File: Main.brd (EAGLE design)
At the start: 100 x 80 mm, 27 parts, among them U1 L298, U2 LM 1084 IT5,0, U3 LM 1084 IT3,3, U4 L298, X1 Motors, X3 Battery

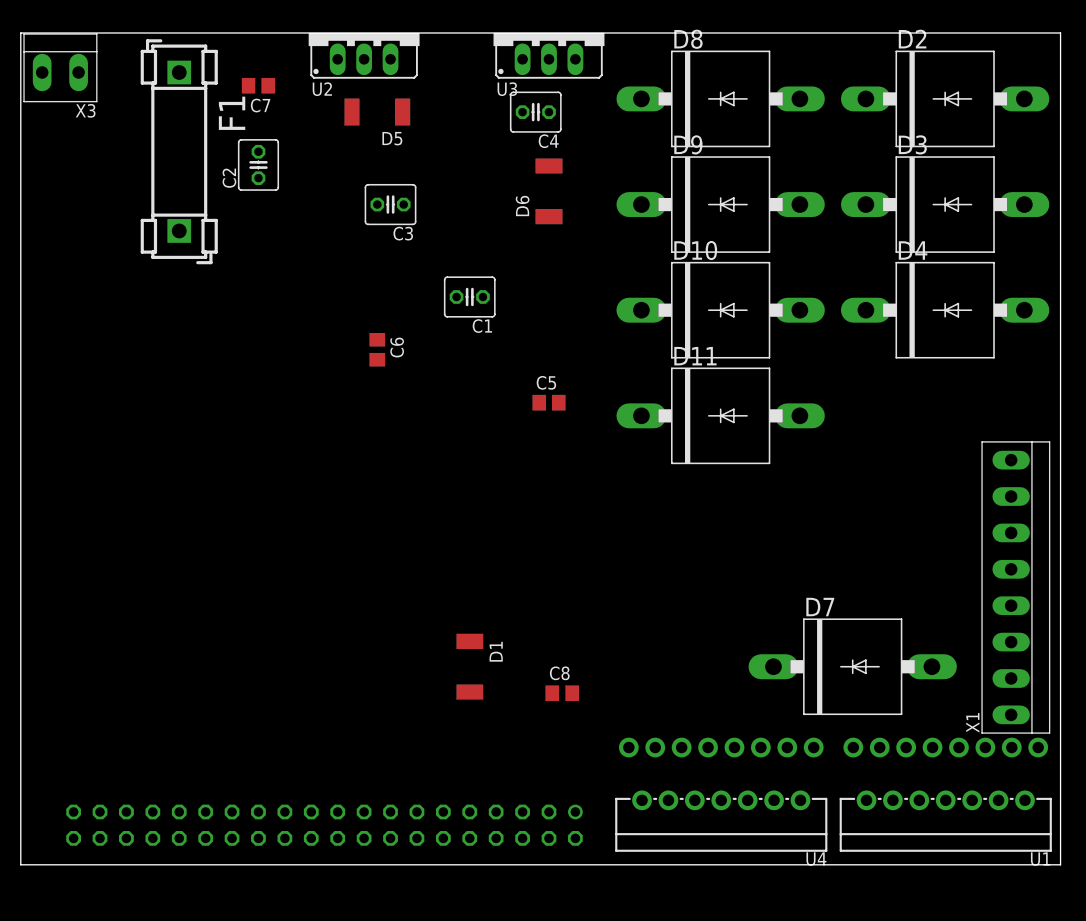
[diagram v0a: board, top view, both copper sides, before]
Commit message: got board working again
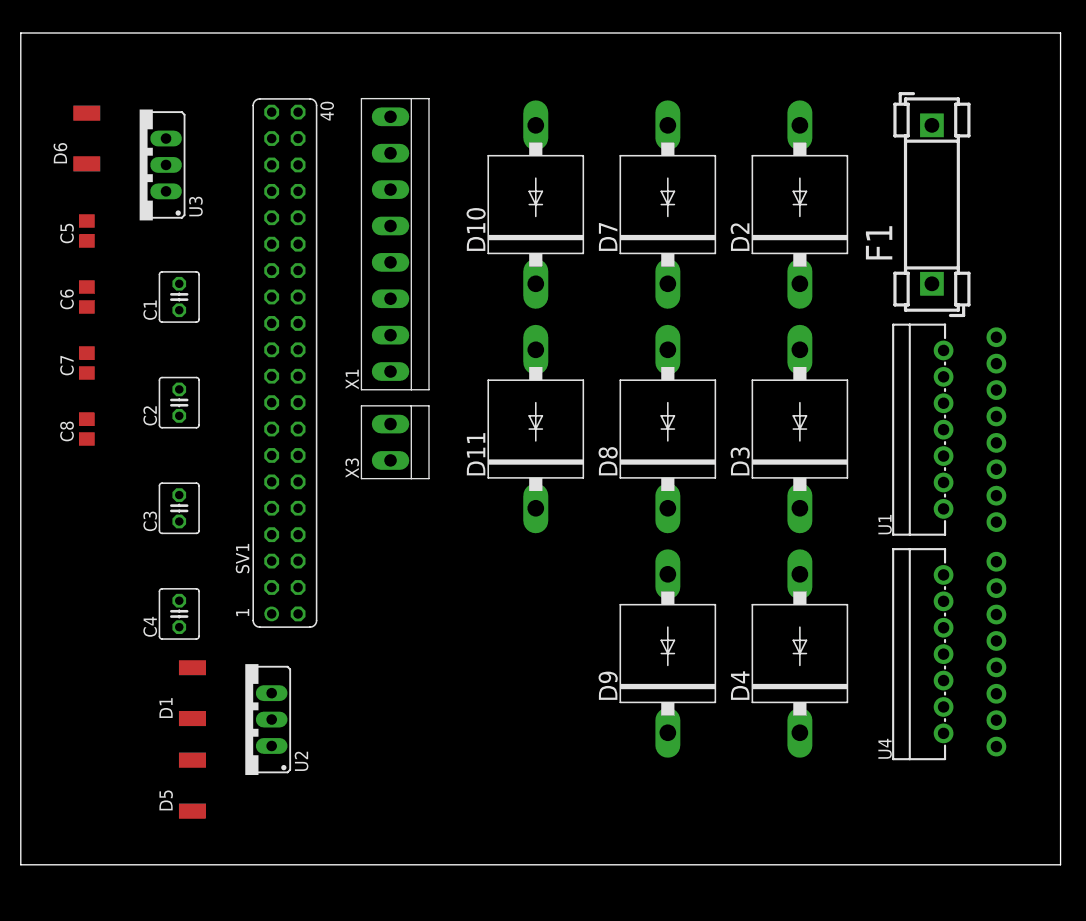
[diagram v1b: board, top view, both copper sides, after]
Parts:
- moved F1 75.2 mm to (87.6, 55.9), turned to 90 degrees
- moved X1 68.2 mm to (35.6, 59.7)
- moved D5 67.2 mm to (16.5, 7.62), turned to 90 degrees
- moved U2 67.0 mm to (21.6, 14.0), turned to 90 degrees
- moved C4 59.2 mm to (15.2, 24.1), turned to 90 degrees
- moved C8 52.3 mm to (6.35, 41.9), turned to 90 degrees
- moved D7 47.9 mm to (62.2, 63.5), turned to 90 degrees
- moved X3 47.7 mm to (35.6, 40.6), turned to 90 degrees
- moved C5 47.4 mm to (6.35, 61.0), turned to 90 degrees
- moved D6 44.7 mm to (6.35, 69.8)
- moved SV1 44.6 mm to (25.4, 48.3), flipped to the top, turned to 90 degrees
- moved D9 43.5 mm to (62.2, 20.3), turned to 90 degrees
- moved U3 41.4 mm to (11.4, 67.3), turned to 90 degrees
- moved D4 35.9 mm to (74.9, 20.3), turned to 90 degrees
- moved C3 35.6 mm to (15.2, 34.3), turned to 90 degrees
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
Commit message: better protection for reverse polarity
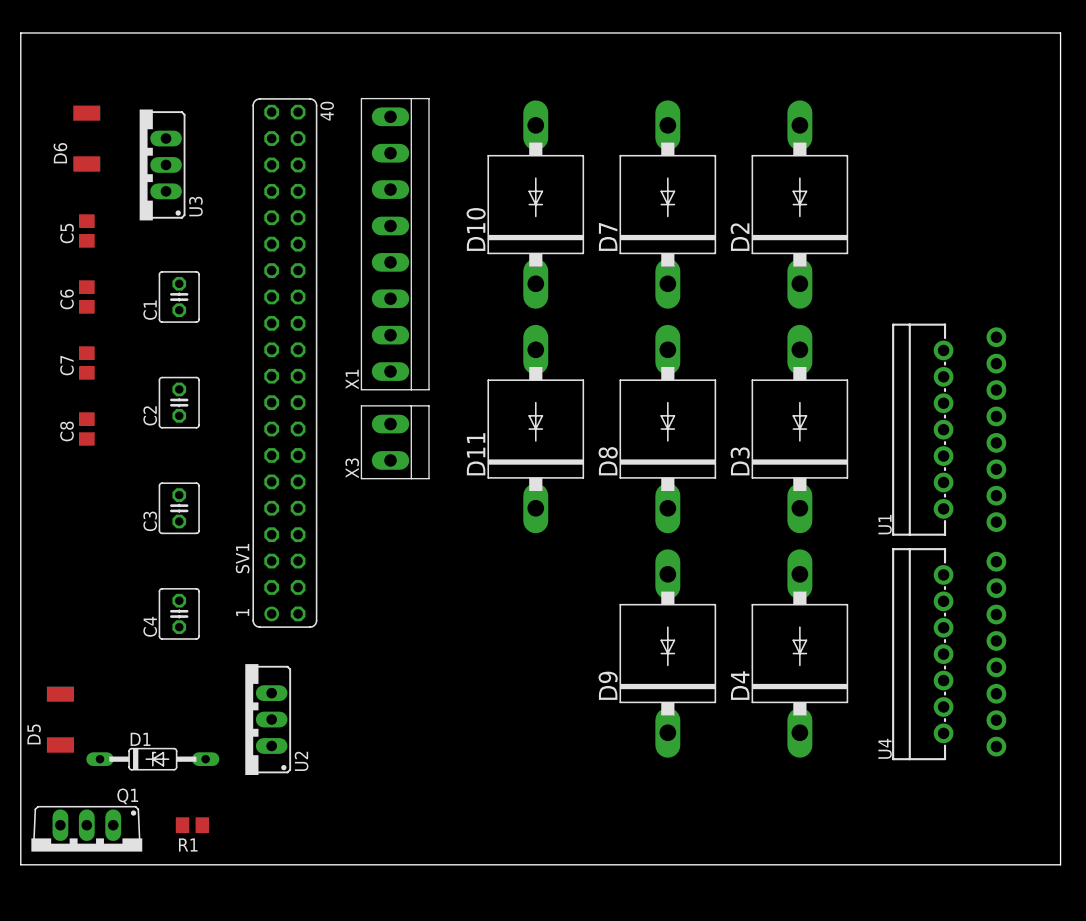
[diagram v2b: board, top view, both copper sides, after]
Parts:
- removed F1: 10A, fuse:FUSE_HOLDER_5X20MM
- added Q1: IRF9530, transistor-power:TO220BV
- added R1: 100k, resistor:R0805
- D1: value 1N4007 -> ZPD15; device semicon-smd-ipc:MELF-MLL41 -> diode:DO35Z10
- D10, D11, D2, D3, D4, D7, D8, D9: value 1N4007 -> P600
- moved D5 14.2 mm to (3.81, 14.0)
- moved D1 7.41 mm to (12.7, 10.2), turned to 0 degrees
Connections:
- new net N$2: D1.A, Q1.G, R1.2
- net +12V: now also Q1.S; no longer D1.1, F1.2
- net GND: now also R1.1; no longer D1.2
- net N$1: now also D1.C, Q1.D; no longer F1.1
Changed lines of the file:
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@@
 <element name="C7" library="rcl" package="C0805" value="100nF" x="6.35" y="48.26" rot="R90"/>
 <element name="C8" library="rcl" package="C0805" value="100nF" x="6.35" y="41.91" rot="R90"/>
-<element name="D1" library="semicon-smd-ipc" package="MELF-MLL41" value="1N4007" x="16.51" y="16.51" rot="R90"/>
-<element name="D10" library="diode" package="P6-15" value="1N4007" x="49.53" y="63.5" rot="R90"/>
-<element name="D11" library="diode" package="P6-15" value="1N4007" x="49.53" y="41.91" rot="R90"/>
-<element name="D2" library="diode" package="P6-15" value="1N4007" x="74.93" y="63.5" rot="R90"/>
-<element name="D3" library="diode" package="P6-15" value="1N4007" x="74.93" y="41.91" rot="R90"/>
-<element name="D4" library="diode" package="P6-15" value="1N4007" x="74.93" y="20.32" rot="R90"/>
-<element name="D5" library="semicon-smd-ipc" package="MELF-MLL41" value="1N4007" x="16.51" y="7.62" rot="R90"/>
+<element name="D10" library="diode" package="P6-15" value="P600" x="49.53" y="63.5" rot="R90"/>
+<element name="D11" library="diode" package="P6-15" value="P600" x="49.53" y="41.91" rot="R90"/>
+<element name="D2" library="diode" package="P6-15" value="P600" x="74.93" y="63.5" rot="R90"/>
+<element name="D3" library="diode" package="P6-15" value="P600" x="74.93" y="41.91" rot="R90"/>
+<element name="D4" library="diode" package="P6-15" value="P600" x="74.93" y="20.32" rot="R90"/>
+<element name="D5" library="semicon-smd-ipc" package="MELF-MLL41" value="1N4007" x="3.81" y="13.97" rot="R90"/>
 <element name="D6" library="semicon-smd-ipc" package="MELF-MLL41" value="1N4007" x="6.35" y="69.85" rot="R90"/>
-<element name="D7" library="diode" package="P6-15" value="1N4007" x="62.23" y="63.5" rot="R90"/>
-<element name="D8" library="diode" package="P6-15" value="1N4007" x="62.23" y="41.91" rot="R90"/>
-<element name="D9" library="diode" package="P6-15" value="1N4007" x="62.23" y="20.32" rot="R90"/>
-<element name="F1" library="fuse" package="FUSE_HOLDER_5X20MM" value="10A" x="87.63" y="55.88" rot="R90">
-<attribute name="OC_NEWARK" value="unknown" x="87.63" y="55.88" size="1.778" layer="27" rot="R90" display="off"/>
-<attribute name="MPN" value="" x="87.63" y="55.88" size="1.778" layer="27" rot="R90" display="off"/>
-<attribute name="MF" value="" x="87.63" y="55.88" size="1.778" layer="27" rot="R90" display="off"/>
-<attribute name="OC_FARNELL" value="unknown" x="87.63" y="55.88" size="1.778" layer="27" rot="R90" display="off"/>
-</element>
+<element name="D7" library="diode" package="P6-15" value="P600" x="62.23" y="63.5" rot="R90"/>
+<element name="D8" library="diode" package="P6-15" value="P600" x="62.23" y="41.91" rot="R90"/>
+<element name="D9" library="diode" package="P6-15" value="P600" x="62.23" y="20.32" rot="R90"/>
 <element name="SV1" library="con-lsta" package="FE20-2" value="Raspberry Pi B Plus Connector" x="25.4" y="48.26" rot="R90">
 <attribute name="OC_NEWARK" value="unknown" x="25.4" y="48.26" size="1.778" layer="27" rot="R90" display="off"/>
@@
 <element name="X1" library="con-ria-59" package="8POL35" value="Motors" x="35.56" y="59.69" rot="R90"/>
 <element name="X3" library="con-ria-59" package="2POL35" value="Battery" x="35.56" y="40.64" rot="R90"/>
+<element name="Q1" library="transistor-power" package="TO220BV" value="IRF9530" x="6.35" y="1.27" rot="R180"/>
+<element name="R1" library="resistor" package="R0805" value="100k" x="16.51" y="3.81" rot="R180"/>
+<element name="D1" library="diode" package="DO35Z10" value="ZPD15" x="12.7" y="10.16"/>
 </elements>
 <signals>
@@
 <wire x1="93.83" y1="21.53" x2="93.83" y2="43.12" width="0" layer="19" extent="1-1"/>
 <wire x1="24.13" y1="13.97" x2="93.83" y2="21.53" width="0" layer="19" extent="1-1"/>
-<wire x1="16.51" y1="10.065" x2="24.13" y2="13.97" width="0" layer="19" extent="1-1"/>
+<wire x1="3.81" y1="16.415" x2="24.13" y2="13.97" width="0" layer="19" extent="1-1"/>
 <wire x1="15.24" y1="43.18" x2="24.13" y2="13.97" width="0" layer="19" extent="1-1"/>
 <wire x1="6.35" y1="40.96" x2="15.24" y2="43.18" width="0" layer="19" extent="1-1"/>
@@
 <contactref element="D5" pad="1"/>
 <contactref element="U2" pad="3"/>
-<contactref element="D1" pad="1"/>
-<contactref element="F1" pad="2"/>
 <contactref element="C1" pad="1"/>
 <contactref element="C3" pad="1"/>
@@
 <contactref element="D9" pad="C"/>
 <contactref element="D8" pad="C"/>
-<wire x1="74.93" y1="55.88" x2="87.63" y2="71.12" width="0" layer="19" extent="1-1"/>
+<contactref element="Q1" pad="S"/>
 <wire x1="74.93" y1="34.29" x2="74.93" y2="55.88" width="0" layer="19" extent="1-1"/>
 <wire x1="62.23" y1="34.29" x2="74.93" y2="34.29" width="0" layer="19" extent="1-1"/>
@@
 <wire x1="62.23" y1="12.7" x2="62.23" y2="34.29" width="0" layer="19" extent="1-1"/>
 <wire x1="24.13" y1="16.51" x2="62.23" y2="12.7" width="0" layer="19" extent="1-1"/>
-<wire x1="16.51" y1="14.065" x2="24.13" y2="16.51" width="0" layer="19" extent="1-1"/>
-<wire x1="16.51" y1="5.175" x2="16.51" y2="14.065" width="0" layer="19" extent="1-1"/>
+<wire x1="3.81" y1="11.525" x2="24.13" y2="16.51" width="0" layer="19" extent="1-1"/>
+<wire x1="3.81" y1="3.81" x2="3.81" y2="11.525" width="0" layer="19" extent="1-1"/>
 <wire x1="15.24" y1="33.02" x2="24.13" y2="16.51" width="0" layer="19" extent="1-1"/>
 <wire x1="6.35" y1="47.31" x2="15.24" y2="33.02" width="0" layer="19" extent="1-1"/>
@@
 </signal>
 <signal name="N$1">
-<contactref element="F1" pad="1"/>
 <contactref element="X3" pad="1"/>
-<wire x1="35.56" y1="38.89" x2="87.63" y2="55.88" width="0" layer="19" extent="1-1"/>
+<contactref element="Q1" pad="D"/>
+<contactref element="D1" pad="C"/>
+<wire x1="6.35" y1="3.81" x2="35.56" y2="38.89" width="0" layer="19" extent="1-1"/>
+<wire x1="7.62" y1="10.16" x2="6.35" y2="3.81" width="0" layer="19" extent="1-1"/>
 </signal>
 <signal name="GND">
@@
 <contactref element="C2" pad="2"/>
 <contactref element="C4" pad="2"/>
-<contactref element="D1" pad="2"/>
 <contactref element="C1" pad="2"/>
 <contactref element="C3" pad="2"/>
@@
 <contactref element="D10" pad="A"/>
 <contactref element="D11" pad="A"/>
+<contactref element="R1" pad="1"/>
 <wire x1="49.53" y1="71.12" x2="62.23" y2="71.12" width="0" layer="19" extent="1-1"/>
 <wire x1="49.53" y1="49.53" x2="49.53" y2="71.12" width="0" layer="19" extent="1-1"/>
@@
 <wire x1="26.67" y1="29.21" x2="35.56" y2="42.39" width="0" layer="19" extent="1-1"/>
 <wire x1="15.24" y1="25.4" x2="26.67" y2="29.21" width="0" layer="19" extent="1-1"/>
-<wire x1="16.51" y1="18.955" x2="15.24" y2="25.4" width="0" layer="19" extent="1-1"/>
 <wire x1="15.24" y1="35.56" x2="15.24" y2="25.4" width="0" layer="19" extent="1-1"/>
 <wire x1="15.24" y1="45.72" x2="15.24" y2="35.56" width="0" layer="19" extent="1-1"/>
@@
 <wire x1="13.97" y1="64.77" x2="6.35" y2="61.91" width="0" layer="19" extent="1-1"/>
 <wire x1="15.24" y1="55.88" x2="6.35" y2="55.56" width="0" layer="19" extent="1-1"/>
-<wire x1="24.13" y1="11.43" x2="16.51" y2="18.955" width="0" layer="19" extent="1-1"/>
+<wire x1="24.13" y1="11.43" x2="15.24" y2="25.4" width="0" layer="19" extent="1-1"/>
+<wire x1="17.46" y1="3.81" x2="24.13" y2="11.43" width="0" layer="19" extent="1-1"/>
 <wire x1="74.93" y1="27.94" x2="49.53" y2="49.53" width="0" layer="19" extent="1-1"/>
 <wire x1="88.75" y1="20.26" x2="74.93" y2="27.94" width="0" layer="19" extent="1-1"/>
@@
 <wire x1="35.56" y1="71.94" x2="35.56" y2="64.94" width="0" layer="19" extent="1-1"/>
 </signal>
+<signal name="N$2">
+<contactref element="R1" pad="2"/>
+<contactref element="Q1" pad="G"/>
+<contactref element="D1" pad="A"/>
+<wire x1="8.89" y1="3.81" x2="15.56" y2="3.81" width="0" layer="19" extent="1-1"/>
+<wire x1="17.78" y1="10.16" x2="15.56" y2="3.81" width="0" layer="19" extent="1-1"/>
+</signal>
 </signals>

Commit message: added PIRs
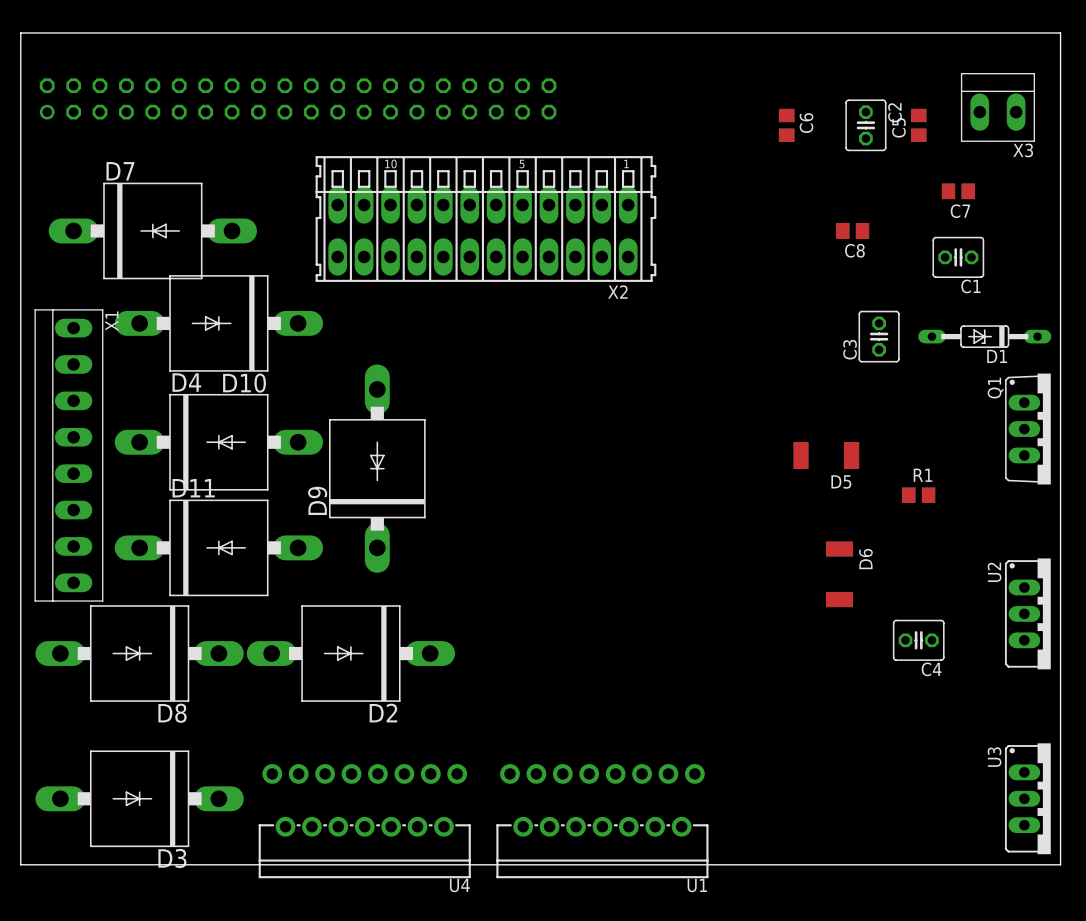
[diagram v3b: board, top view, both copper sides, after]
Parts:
- added X2: (no value), con-wago:233-512
- moved U3 106.7 mm to (99.1, 6.35), turned to 270 degrees
- moved Q1 101.2 mm to (99.1, 41.9), turned to 270 degrees
- moved D1 89.7 mm to (92.7, 50.8), turned to 180 degrees
- moved C7 85.4 mm to (90.2, 64.8), turned to 180 degrees
- moved D6 83.6 mm to (78.7, 27.9), turned to 270 degrees
- moved C5 80.7 mm to (86.4, 71.1)
- moved U2 78.1 mm to (99.1, 24.1), turned to 270 degrees
- moved D5 77.9 mm to (77.5, 39.4), turned to 180 degrees
- moved R1 76.7 mm to (86.4, 35.6), turned to 0 degrees
- moved C8 76.1 mm to (80.0, 61.0), turned to 180 degrees
- moved C1 75.0 mm to (90.2, 58.4), turned to 180 degrees
- moved D3 72.8 mm to (11.4, 6.35), turned to 180 degrees
- moved C2 71.2 mm to (81.3, 71.1), turned to 270 degrees
- moved C4 71.2 mm to (86.4, 21.6), turned to 180 degrees
- moved C3 69.3 mm to (82.5, 50.8)
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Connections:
- new net PIR1: X2.B2
- new net PIR2: X2.B5
- new net PIR3: X2.B8
- new net PIR4: X2.B11
- net +5V: now also X2.B12, X2.B3, X2.B6, X2.B9
- net GND: now also X2.B1, X2.B10, X2.B4, X2.B7

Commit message: connections to RPI
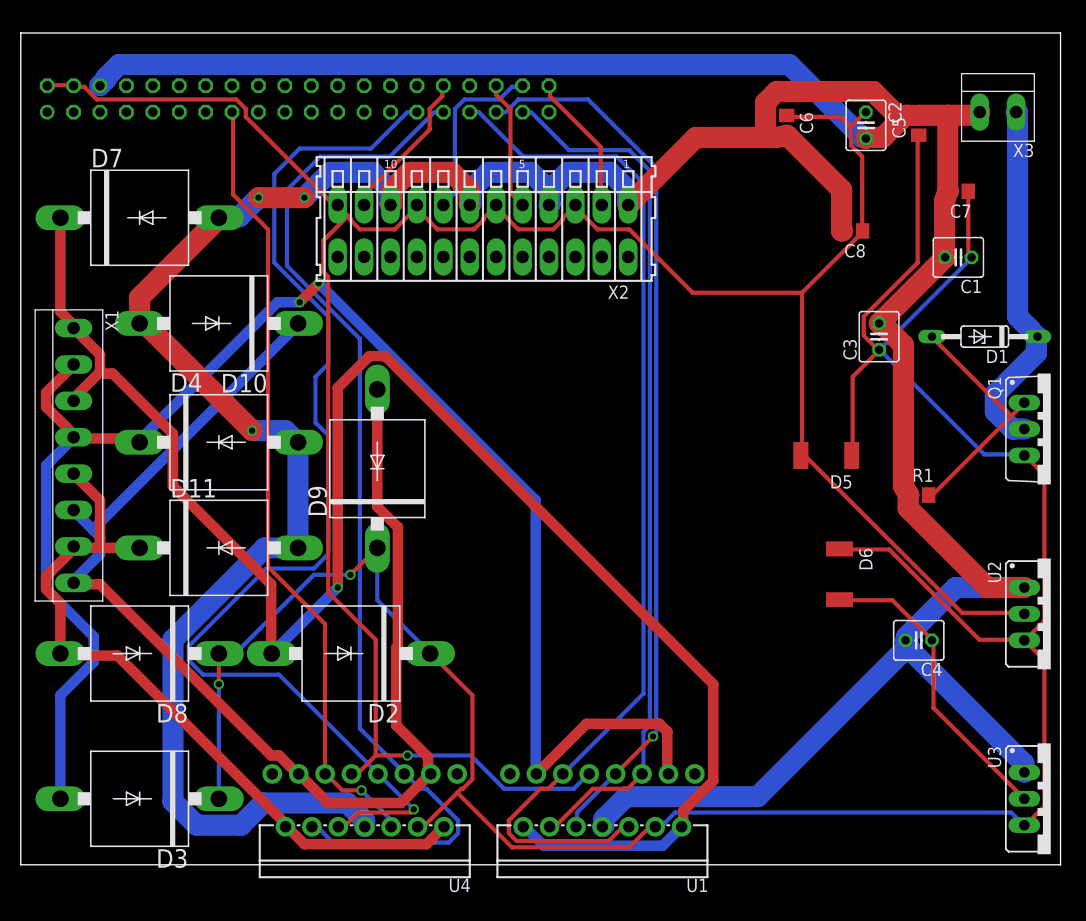
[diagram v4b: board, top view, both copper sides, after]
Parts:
- X2: value (none) -> PIRs
- moved D7 1.80 mm to (11.4, 62.2)
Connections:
- new net N$10: SV1.26
- new net N$11: SV1.24
- new net N$12: SV1.22
- new net N$13: SV1.20
- new net N$14: SV1.18
- new net N$15: SV1.16
- new net N$17: SV1.12
- new net N$18: SV1.10
- new net N$19: SV1.8
- new net N$20: SV1.3
- new net N$21: SV1.5
- new net N$22: SV1.7
- new net N$23: SV1.9
- new net N$24: SV1.11
- new net N$25: SV1.13
- new net N$27: SV1.17
- new net N$28: SV1.19
- new net N$29: SV1.21
- new net N$3: SV1.14
- new net N$30: SV1.23
- new net N$31: SV1.25
- new net N$32: SV1.27
- new net N$38: SV1.39
- new net N$6: SV1.34
- new net N$8: SV1.30
- new net N$9: SV1.28
- net +5V: now also SV1.2, SV1.4
- net ML_A: now also SV1.37
- net ML_B: now also SV1.35
- net ML_PWM: now also SV1.33
- net MR_A: now also SV1.31
- net MR_B: now also SV1.29
- net MR_PWM: now also SV1.15
- net PIR1: now also SV1.40
- net PIR2: now also SV1.36
- net PIR3: now also SV1.38
- net PIR4: now also SV1.32
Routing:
- net GND: track 0.00 -> 411.9 mm, vias 0 -> 3
- net +12V: track 0.00 -> 257.6 mm, vias 0 -> 2
- net +5V: track 0.00 -> 239.7 mm, vias 0 -> 1
- net ML_OUT_A: track 0.00 -> 165.1 mm, vias 0 -> 1
- net ML_OUT_B: track 0.00 -> 153.3 mm, vias 0 -> 2
- net MR_OUT_B: track 0.00 -> 120.6 mm
- net MR_B: track 0.00 -> 109.9 mm, vias 0 -> 1
- net MR_A: track 0.00 -> 102.3 mm
- net ML_PWM: track 0.00 -> 100.3 mm
- net ML_B: track 0.00 -> 85.2 mm, vias 0 -> 1
- net ML_A: track 0.00 -> 84.0 mm
- net MR_PWM: track 0.00 -> 76.2 mm, vias 0 -> 1
- net MR_OUT_A: track 0.00 -> 71.8 mm
- net N$1: track 0.00 -> 34.9 mm
- net +3.3V: track 0.00 -> 29.5 mm
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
